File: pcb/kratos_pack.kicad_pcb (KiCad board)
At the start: 4 copper layers, 44.2 x 20.2 mm, 120 parts, among them J1 USB_C_Receptacle_USB2.0, J2 PROG_CONN, J3 DBG_UART, J4 BAT_MID+NTC, J5 BAT_7.4V, J6 BAT_0V, J7 OUT+, J8 OUT-, Q1 AON7403, Q2 AON7414, Q3 AON7414, Q4 UT6MA2TCR, Q5 UT6MA2TCR, Q6 UT6MA2TCR, SW1 WAKEUP, SW2 BOOT, SW3 RST_BTN, U1 USBLC6-2SC6, U10 24LC32, U11 MIC94300, U12 74LVC2G14, U13 MIC94300, U2 CP2102N-Axx-xQFN20, U3 STM32G071Gx, U4 KTD2026BEWE, U5 BQ25887, U6 BD48xxFVE, U7 INA199, U8 LTC4231, U9 LDK715M33R

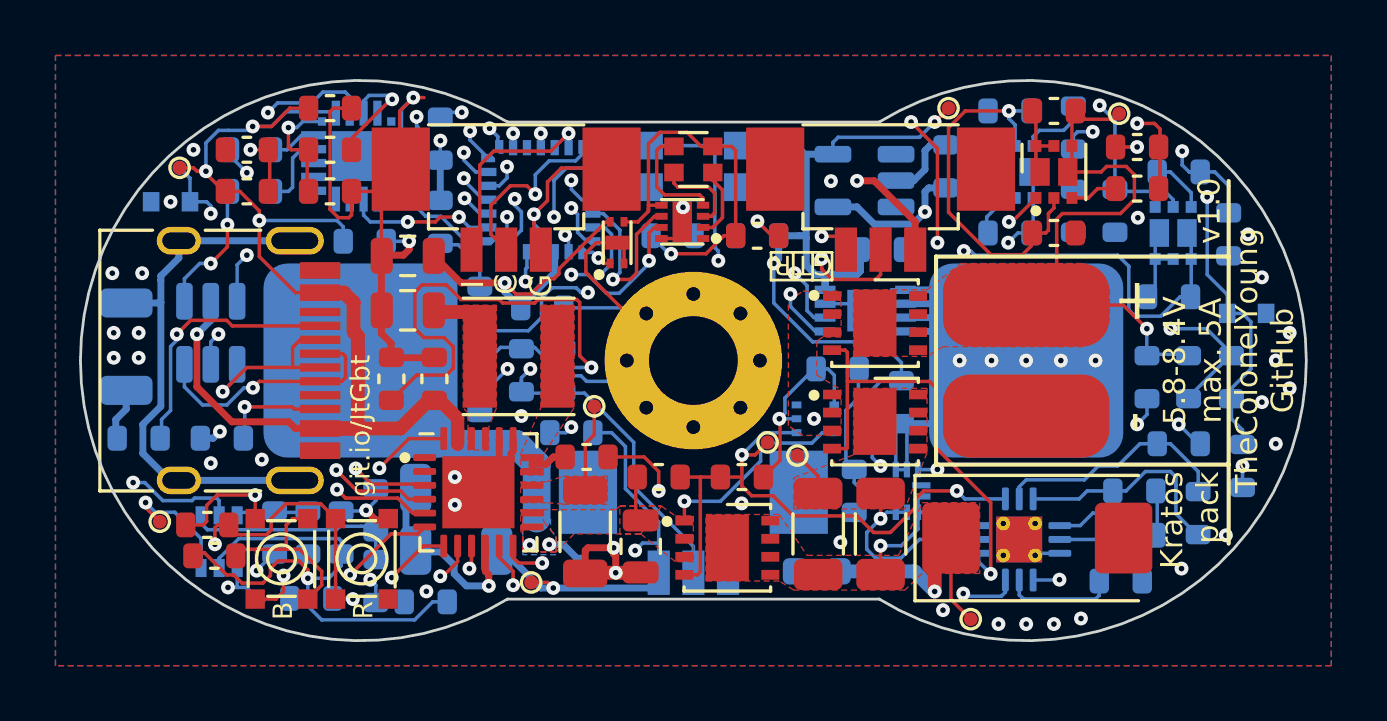
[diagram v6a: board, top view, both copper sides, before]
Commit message: Schema & PCB: fix under-voltage supervisor by inverting output signal
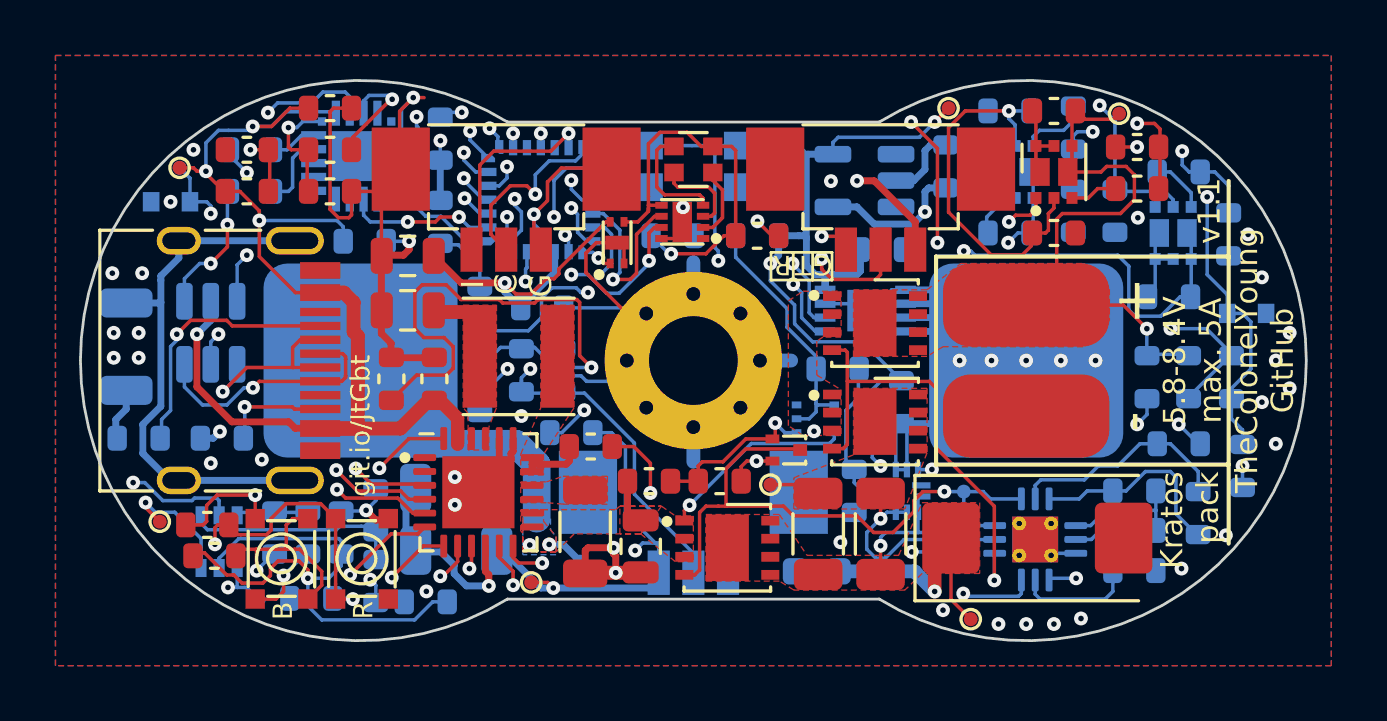
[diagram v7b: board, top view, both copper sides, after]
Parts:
- removed TP4: SNS, TCY_connectors:TestPoint_Pad_D0.5mm
- added Q7: DMN2450UFD, TCY_IC:DFN-3_1.2x1.2mm, F.Cu at (154.3, 103.2)
- added R19: 470k, TCY_passives:R_0603_1608Metric, F.Cu at (149.4, 104.3)
- R31, TP8: moved to B.Cu
- moved R31 11.0 mm to (160.5, 106.4), turned to 90 degrees
- moved TP8 7.29 mm to (160.8, 104.7), turned to 180 degrees
- moved TP7 1.43 mm to (153.8, 104.5)
- moved C19 0.81 mm to (151.9, 104.3)
- moved C20 0.62 mm to (166.9, 107.6)
- moved U8 0.57 mm to (163.3, 106.5)
- moved C9 0.40 mm to (147.3, 103.1)
- moved R30 0.17 mm to (166.9, 106.1)
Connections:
- C19 pad 1: /UVLO -> Net-(U6-Pad1)
- U6 pad 1: /UVLO -> Net-(U6-Pad1)
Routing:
- net GND: track 154.0 -> 168.6 mm, vias 55 -> 54
- net /VBAT: track 56.6 -> 66.4 mm, vias 4 -> 5
- net Net-(U6-Pad1): track 0.00 -> 6.16 mm, vias 0 -> 1
- net /CS_EN: track 29.7 -> 35.1 mm
- net /SNS: track 3.16 -> 0.00 mm
- net Net-(R22-Pad1): track 8.45 -> 9.89 mm
- net Net-(R27-Pad2): track 5.63 -> 4.54 mm
- net Net-(C9-Pad2): track 1.80 -> 2.56 mm
- net /SENSE: track 9.39 -> 10.1 mm
- net /UVLO: track 21.8 -> 21.1 mm, vias 2 -> 1
- net Net-(Q2-Pad1): track 11.7 -> 12.4 mm
- net Net-(R26-Pad2): track 7.96 -> 7.38 mm
- net Net-(R25-Pad2): track 8.62 -> 8.07 mm
- net +3V3: track 89.9 -> 89.4 mm
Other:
- board text added: "v1.1"
- board text removed: "v1.0"

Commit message: PCB: Fixed silkscreen overlapping issues (side button and USB connector)
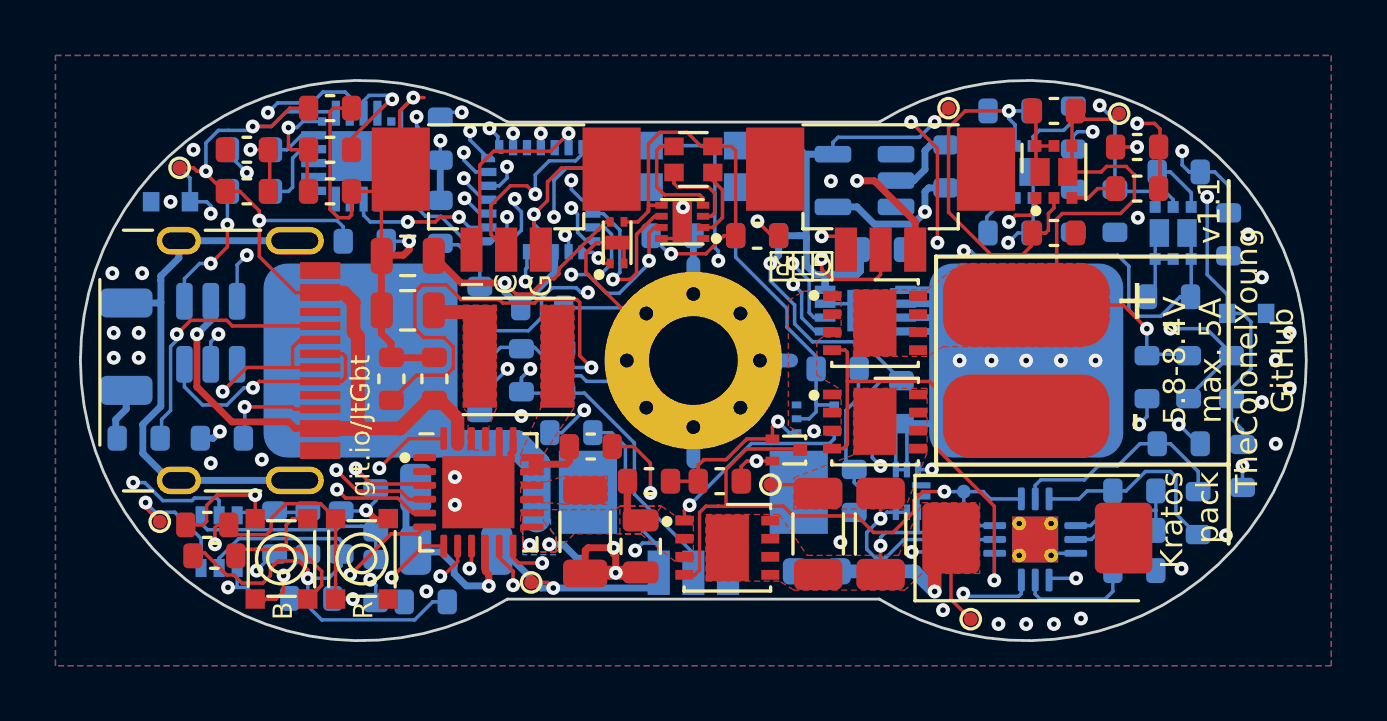
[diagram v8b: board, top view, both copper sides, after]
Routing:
- net GND: track 168.6 -> 169.5 mm
